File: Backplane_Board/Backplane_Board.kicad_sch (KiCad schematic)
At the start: 2 parts

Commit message: added ad converter
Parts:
- added C11, C12, C13, C4, C5: C_Polarized_US, symbol Device:C_Polarized_US
- added D10: ZPDxx, Diode_THT:D_DO-35_SOD27_P10.16mm_Horizontal, symbol Diode:ZPDxx
- added D11: LED, symbol Device:LED
- added J17: Conn_01x02_Pin, symbol Connector:Conn_01x02_Pin
- added R19, R21, R22: R, symbol Device:R
- added R20: 3K, symbol Device:R
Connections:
- new net: D11.1 (K), R20.1
- new net: D10.2 (A), R19.1
- new net 60V: C11.1, C12.1, C13.1, C4.1, C5.1, D10.1 (K), D11.2 (A), J17.1 (Pin_1), R21.1
- new net GND: C11.2, C12.2, C13.2, C4.2, C5.2, J17.2 (Pin_2), R19.2, R20.2, R22.2
- new net batteryVD: R21.2, R22.1
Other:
- added sheet Voltage_Level_ADC (Voltage Level ADC.kicad_sch)
- note added: "indivdual fuses?"
- moved on the sheet: U1, U3

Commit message: add rerevised esc board and rough backplane schmatic
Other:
- added sheet BoardBoardConnections (BoardBoardConnections.kicad_sch)
- note added: "Capactor banks: These need to be broken up/ specfic to the input. All the bricks have diffrent ESR requirments. With the large number of caps on this bus, it should not be a problem though. The main thing that ditates the requirments for the capactance is the indutance of the sorce, and since this is a battery with very thigh cabling, it is hard to imagne there is much at all"
- note added: "Main power input"
- company: (none) -> Cabrillo Robtics
- title: (none) -> Backplane_Board
- moved on the sheet: C11, C12, C13, C4, C5, D10, D11, J17, R19, R20, R21, R22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

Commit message: backup before heavy revtion
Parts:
- removed C11, C12, C13: C_Polarized_US, symbol Device:C_Polarized_US
- removed D10: ZPDxx, Diode_THT:D_DO-35_SOD27_P10.16mm_Horizontal, symbol Diode:ZPDxx
- removed D11: LED, symbol Device:LED
- removed R19, R21, R22: R, symbol Device:R
- removed R20: 3K, symbol Device:R
- removed U1, U3: ~, symbol PKJ7213WPI:PKJ7213WPI
- added D1: LED, symbol Device:LED
- added D2: D, symbol Device:D
- added Q1: Q_NMOS_DGS, symbol Device:Q_NMOS_DGS
- added R5: R, symbol Device:R
- added U1: TCR2EE11, Package_TO_SOT_SMD:SOT-553, symbol Regulator_Linear:TCR2EE11
- C4, C5: value C_Polarized_US -> 330uF
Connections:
- net 60V: now also Q1.1 (D); no longer J17.1 (Pin_1)
- net GND: now also R5.2, U1.2 (GND)
- new net: D2.1 (K), U1.3 (VIN)
- new net: D2.2 (A), J17.1 (Pin_1), Q1.3 (S)
- new net: D1.1 (K), R5.1
- new net: D1.2 (A), Q1.2 (G), U1.4 (VOUT)
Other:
- note added: "Reverse input voltage protection. I did it this way, insted of using a p-chanle becuse will be having varing voltage levels (also need a status LED, so have the ragulator anyways) (to protect the ragulator, we can use a scotty diode)"
- note removed: "indivdual fuses?"
- moved on the sheet: C4, C5

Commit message: back plane board ready for review
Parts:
- added C6: C_Polarized_Small_US, symbol Device:C_Polarized_Small_US
- added JP1: Jumper_2_Open, symbol Jumper:Jumper_2_Open
- added R3, R4, R9: R, symbol Device:R
- added U3: PINA740AIREMR, VQFN14_REM_TEX, symbol INA740BIREMR:PINA740AIREMR
- R5: value R -> 10k
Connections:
- net 60V: now also JP1.2 (B); no longer Q1.1 (D)
- net GND: now also C6.2, U3.12 (GND), U3.7 (IS-)
- new net: U3.1 (SH+), U3.2 (IN+)
- new net: U3.8 (SH-), U3.9 (IN-)
- new net +5V: C6.1, R3.1, R4.1, R9.1, U3.11 (VS)
- new net ALERT: R3.2, U3.10 (ALERT)
- new net SCL: R9.2, U3.6 (SCL)
- new net SDA: R4.2, U3.5 (SDA)
- new net VBUS_IN: JP1.1 (A), Q1.1 (D), U3.13 (VBUS), U3.14 (IS+)
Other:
- removed sheet Voltage_Level_ADC
- note added: "Voltage, Current, Power, Energy Monitoring"
- note added: "do we need a levle shifter to bring this to 3V3?"
- note added: "need to spec this mosfet. I am wondering if this should be a p-chanle mosfet insted, so we are not relying on a cheep liner ragulator to keep our system on?"
- note added: "should we have a tone of JPs or just have a fixed address?"
- moved on the sheet: C4, C5, D1, D2, R5, U1

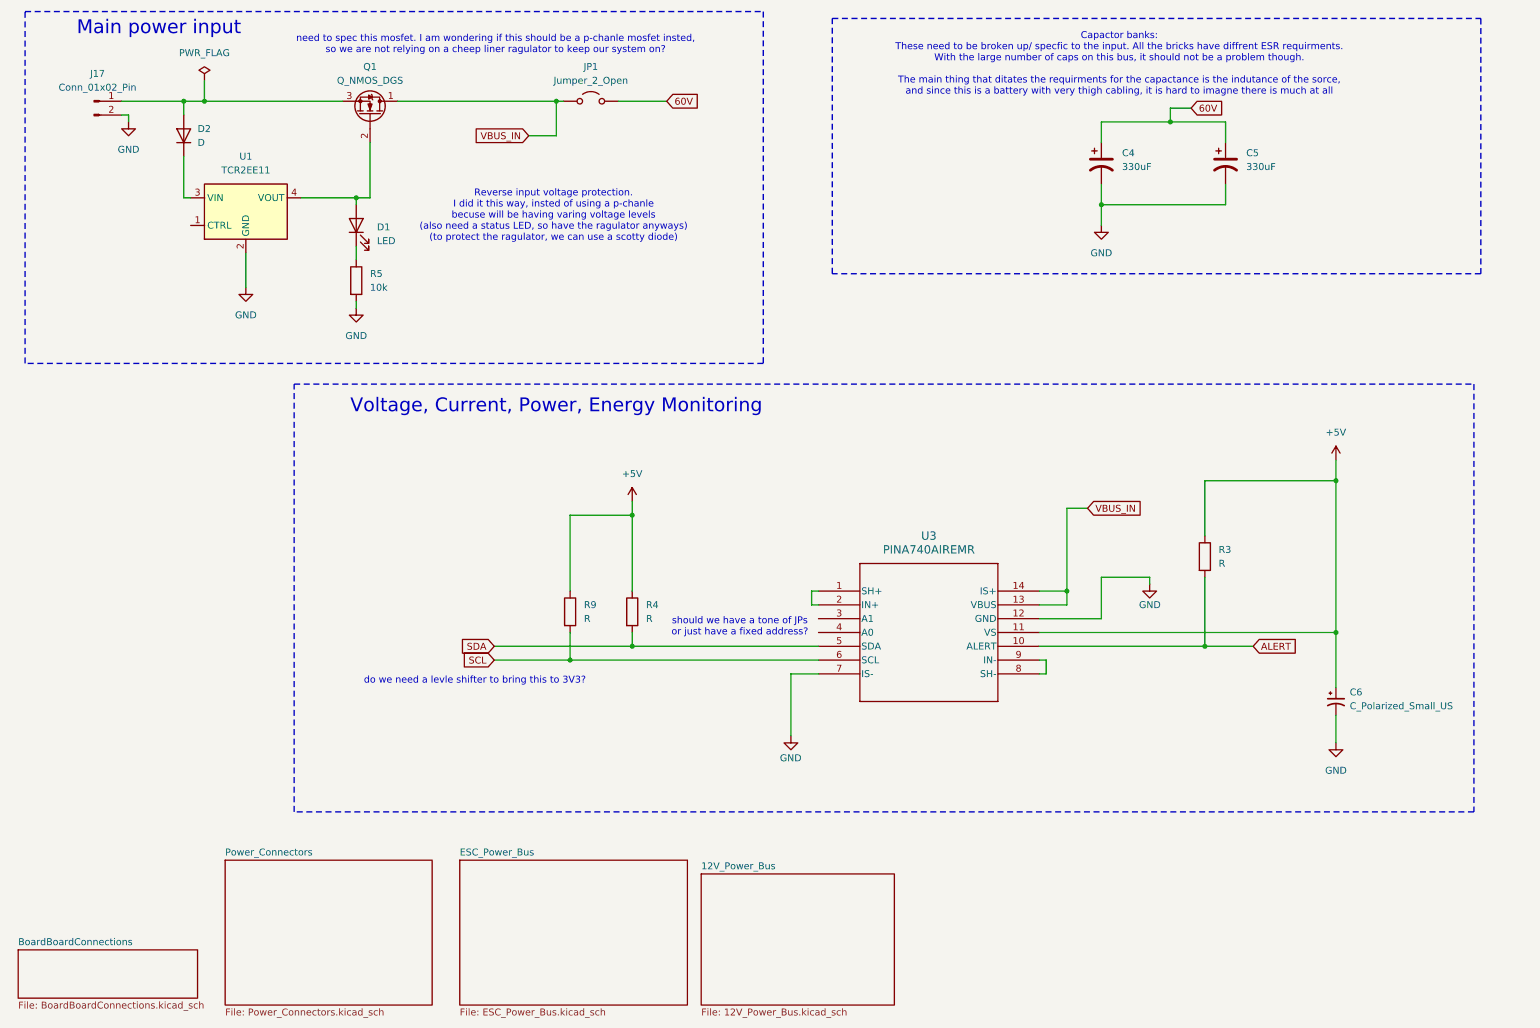
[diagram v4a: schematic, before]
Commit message: updated input revers polarity protection
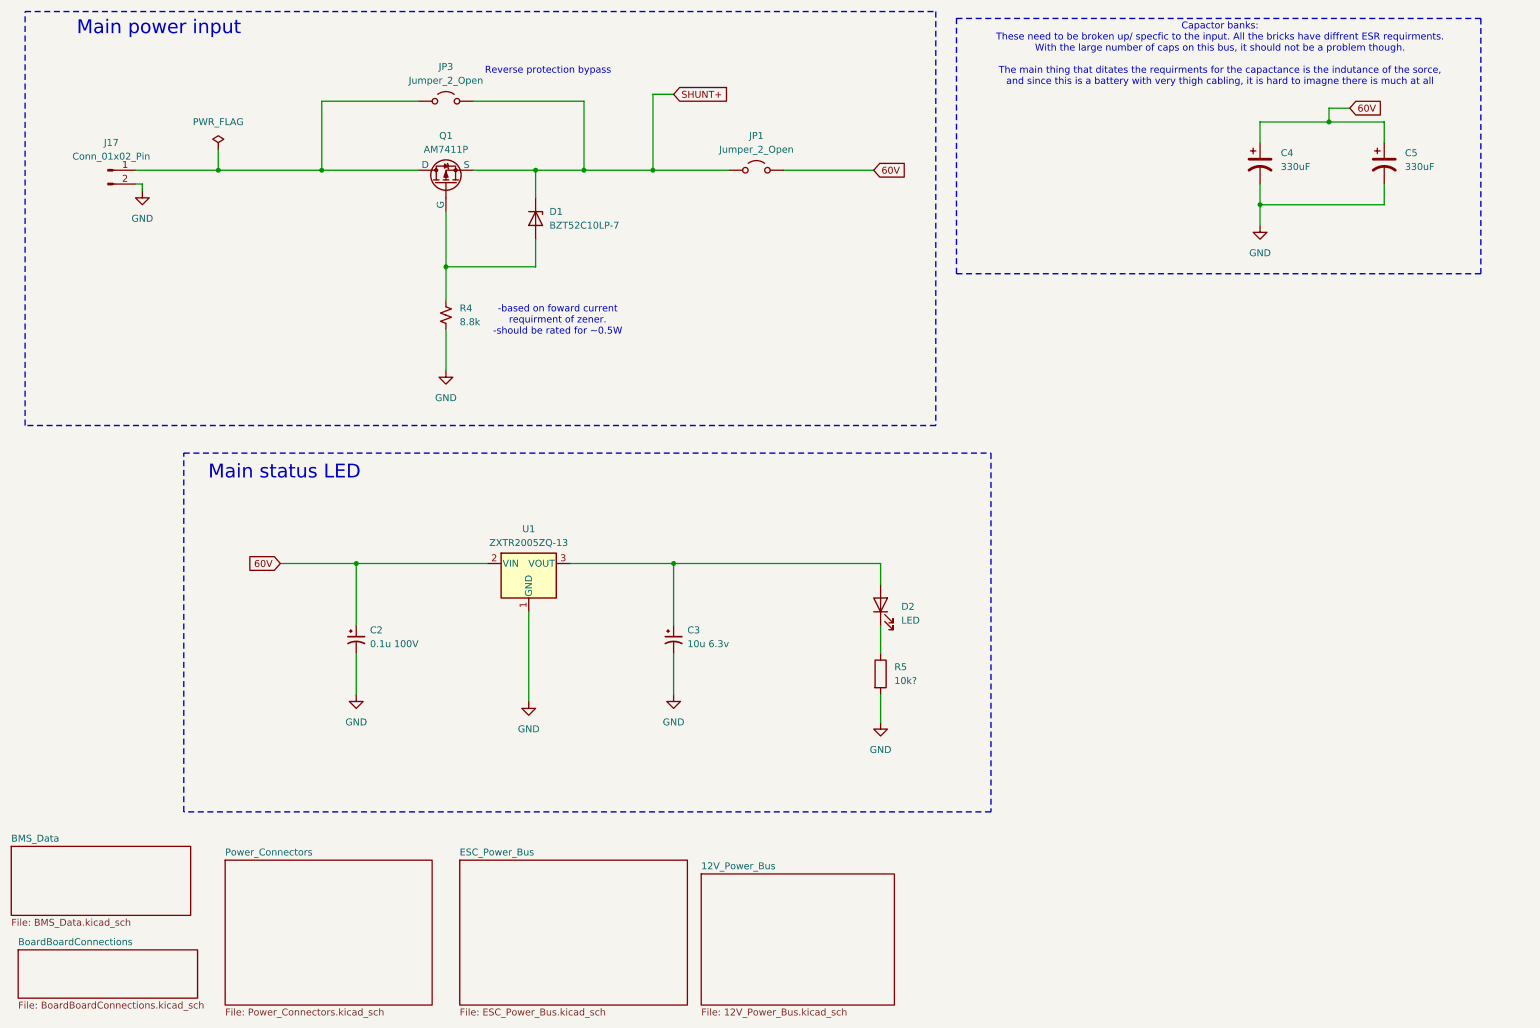
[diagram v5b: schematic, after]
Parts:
- removed C6: C_Polarized_Small_US, symbol Device:C_Polarized_Small_US
- removed D1: LED, symbol Device:LED
- removed D2: D, symbol Device:D
- removed Q1: Q_NMOS_DGS, symbol Device:Q_NMOS_DGS
- removed R3, R4, R9: R, symbol Device:R
- removed U1: TCR2EE11, Package_TO_SOT_SMD:SOT-553, symbol Regulator_Linear:TCR2EE11
- removed U3: PINA740AIREMR, VQFN14_REM_TEX, symbol INA740BIREMR:PINA740AIREMR
- added C2: 0.1u 100V, symbol Device:C_Polarized_Small_US
- added C3: 10u 6.3v, symbol Device:C_Polarized_Small_US
- added D1: BZT52C10LP-7, symbol Device:D_Zener
- added D2: LED, symbol Device:LED
- added JP3: Jumper_2_Open, symbol Jumper:Jumper_2_Open
- added Q1: AM7411P, symbol Simulation_SPICE:PMOS
- added R4: 8.8k, symbol Device:R_Small_US
- added U1: ZXTR2005ZQ-13, symbol Regulator_Linear:AP2127N-1.0
- R5: value 10k -> 10k?
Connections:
- net 60V: now also C2.1, U1.2 (VIN)
- net GND: now also C2.2, C3.2, R4.2, U1.1 (GND)
- net at J17.1 (Pin_1): now also JP3.1 (A), Q1.1 (D)
- net at R5.1: now also D2.1 (K)
- net VBUS_IN renamed SHUNT+
- net SHUNT+: now also D1.1 (K), JP3.2 (B), Q1.3 (S)
- new net: C3.1, D2.2 (A), U1.3 (VOUT)
- new net: D1.2 (A), Q1.2 (G), R4.1
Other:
- added sheet BMS_Data (BMS_Data.kicad_sch)
- note added: "-based on foward current requirment of zener. -should be rated for ~0.5W"
- note added: "Main status LED"
- note added: "Reverse protection bypass"
- note removed: "Reverse input voltage protection. I did it this way, insted of using a p-chanle becuse will be having varing voltage levels (also need a status LED, so have the ragulator anyways) (to protect the ragulator, we can use a scotty diode)"
- note removed: "Voltage, Current, Power, Energy Monitoring"
- note removed: "do we need a levle shifter to bring this to 3V3?"
- note removed: "need to spec this mosfet. I am wondering if this should be a p-chanle mosfet insted, so we are not relying on a cheep liner ragulator to keep our system on?"
- note removed: "should we have a tone of JPs or just have a fixed address?"
- moved on the sheet: C4, C5, J17

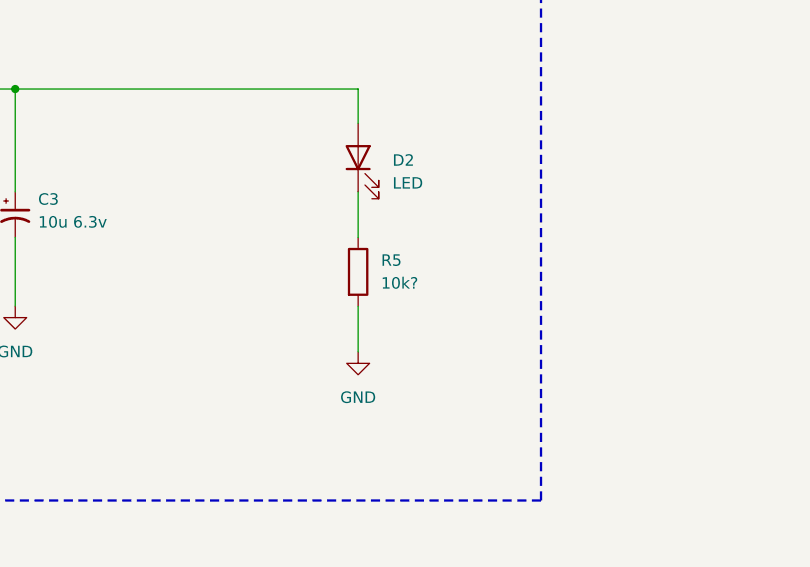
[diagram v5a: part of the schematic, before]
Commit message: reviewed and cleaned up management ic
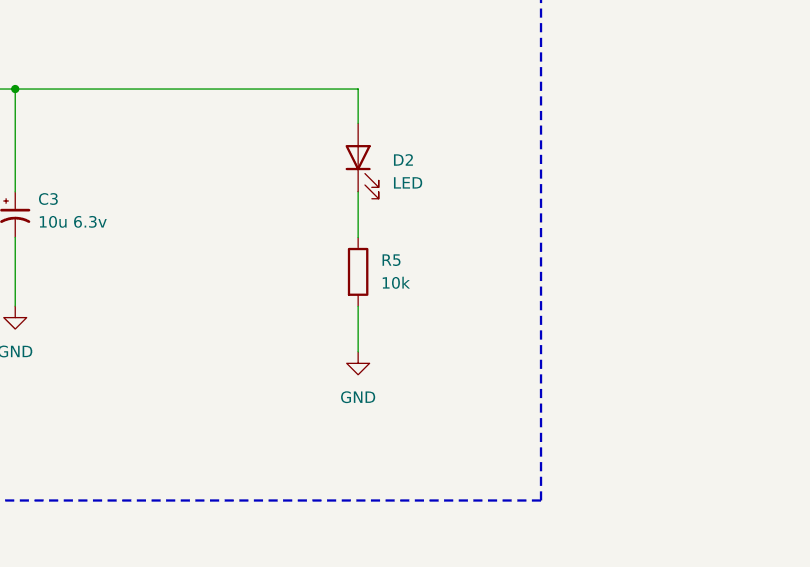
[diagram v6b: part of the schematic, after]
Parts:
- R5: value 10k? -> 10k
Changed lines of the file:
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@@
 			)
 		)
-		(property "Value" "10k?"
+		(property "Value" "10k"
 			(at 175.26 135.8899 0)
 			(effects

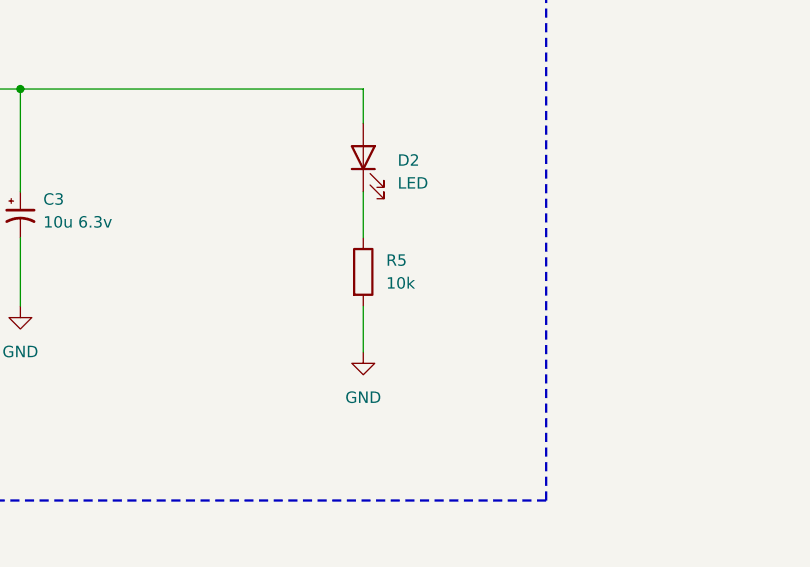
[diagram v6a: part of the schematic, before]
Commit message: added pico and 5v killSW
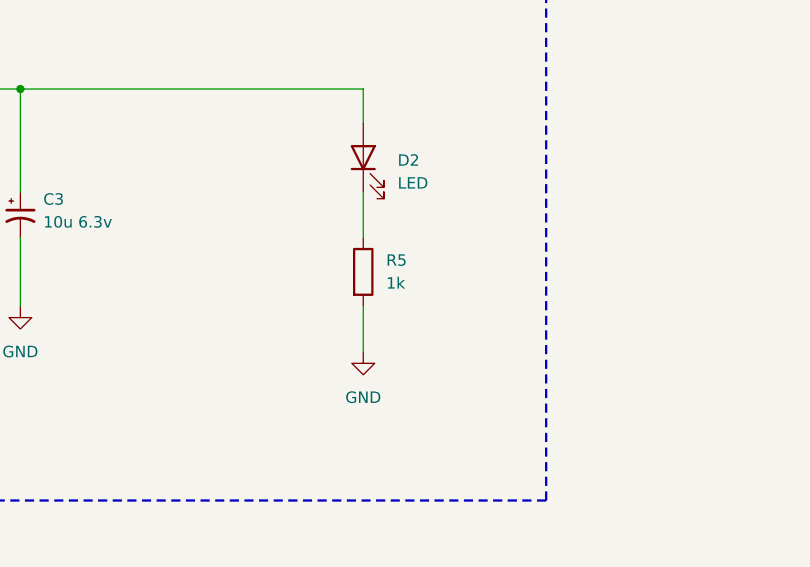
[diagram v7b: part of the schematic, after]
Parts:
- R5: value 10k -> 1k
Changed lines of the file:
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@@
 	(title_block
 		(title "Backplane_Board")
-		(date "2024-09-30")
+		(date "2024-10-29")
 		(rev "1")
 		(company "Cabrillo Robtics")
@@
 			)
 		)
-		(property "Value" "10k"
+		(property "Value" "1k"
 			(at 175.26 135.8899 0)
 			(effects
@@
 			(project "Backplane_Board"
 				(path "/4484cfee-9e43-4cef-88b4-a8ca308542b4"
-					(page "4")
+					(page "5")
 				)
 			)
@@
 			(project "Backplane_Board"
 				(path "/4484cfee-9e43-4cef-88b4-a8ca308542b4"
-					(page "3")
+					(page "4")
 				)
 			)
@@
 			(project "Backplane_Board"
 				(path "/4484cfee-9e43-4cef-88b4-a8ca308542b4"
-					(page "2")
-				)
-			)
+					(page "3")
+				)
+			)

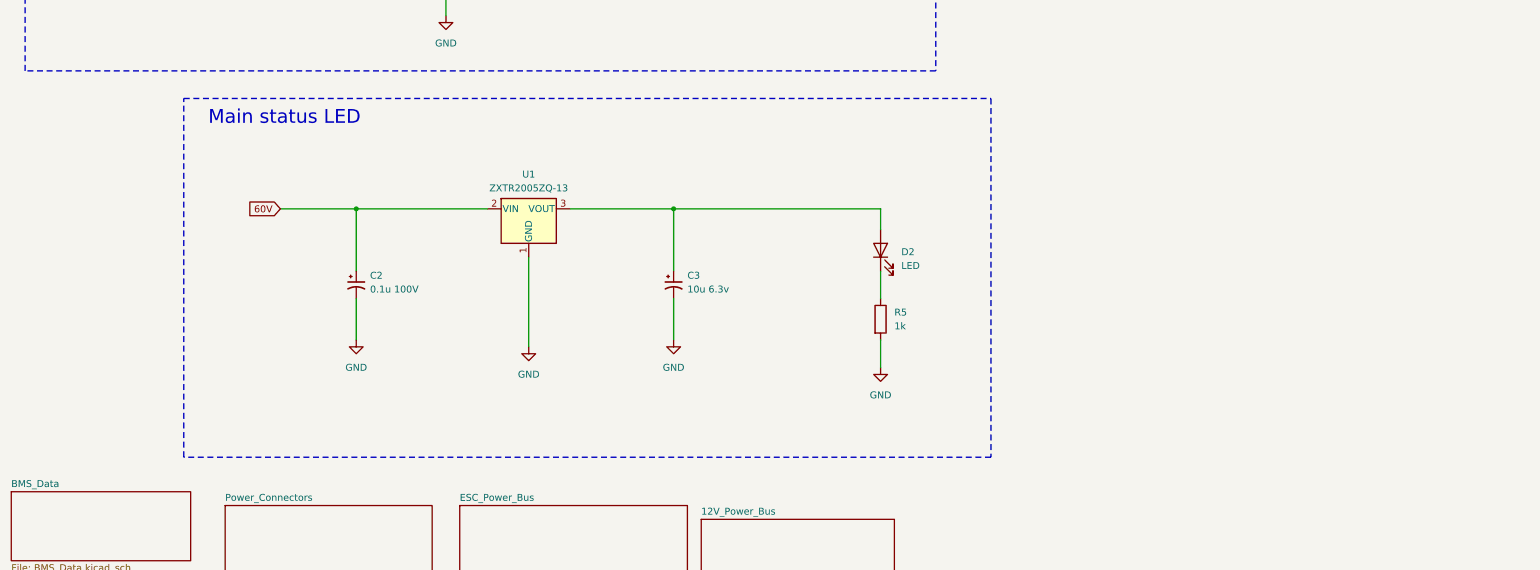
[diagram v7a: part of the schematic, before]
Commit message: added power swtching circits
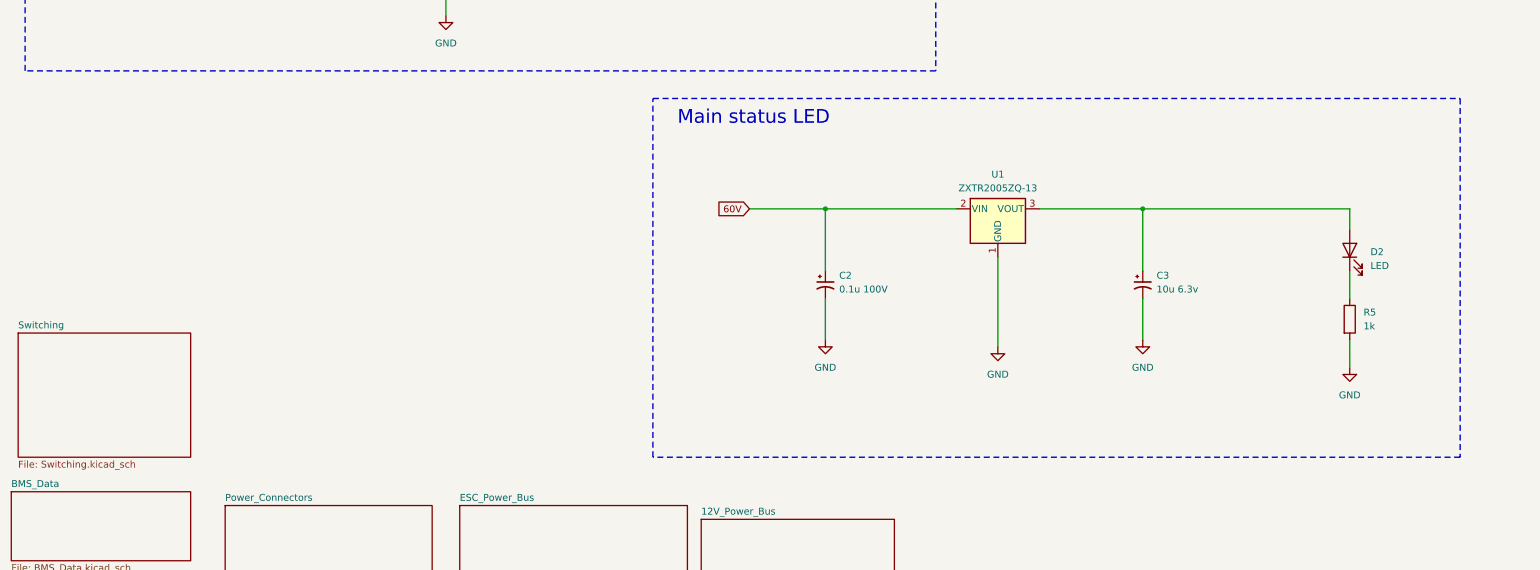
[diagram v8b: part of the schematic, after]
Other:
- added sheet Switching (Switching.kicad_sch)
- moved on the sheet: C2, C3, D2, R5, U1
